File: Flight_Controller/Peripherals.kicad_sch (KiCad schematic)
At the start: 18 parts, among them IC1 AT7456E, U2 BMI270, U4 W25Q128JVSIQ TR, Y2 ABM3-27.000MHZ-D2Y-T

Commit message: Schem V1 Done!
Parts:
- removed R2: 1kΩ, PCM_JLCPCB:R_0603, symbol PCM_JLCPCB-Resistors:0603,1kΩ
- added C10: 33nF, PCM_JLCPCB:C_0603, symbol PCM_JLCPCB-Capacitors:0603,33nF
- added C11, C24, C30, C31, C32, C7: 100nF, PCM_JLCPCB:C_0603, symbol PCM_JLCPCB-Capacitors:0603,100nF
- added C12: 6.8pF, PCM_JLCPCB:C_0603, symbol PCM_JLCPCB-Capacitors:0603,6.8pF
- added C13: 47uF, PCM_JLCPCB:C_0805, symbol PCM_JLCPCB-Capacitors:0805,47uF
- added C14, C15: 1uF, PCM_JLCPCB:C_0603, symbol PCM_JLCPCB-Capacitors:0603,1uF
- added C33: 10uF, PCM_JLCPCB:C_0805, symbol PCM_JLCPCB-Capacitors:0805,10uF,(2)
- added L1: 12uH, symbol Device:L
- added NT1, NT2, NT3, NT4: NetTie_2, symbol Device:NetTie_2
- added R7: 52.3K, symbol Device:R
- added R8: 10kΩ, PCM_JLCPCB:R_0603, symbol PCM_JLCPCB-Resistors:0603,10kΩ
- added U3: TLV75533PDBV, Package_TO_SOT_SMD:SOT-23-5, symbol Regulator_Linear:TLV75533PDBV
- added U5: TPS62932, Package_TO_SOT_SMD:SOT-583-8, symbol Regulator_Switching:TPS62932
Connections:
- net SPI_CLK is gone; now on net SPI_SCK: U4.6 (CLK)
- net SPI_IO0 is gone; now on net SPI_SDI: U4.5 (DI(IO0))
- net +3V3: now also R1.1, R3.1, U2.8 (VDD), C15.1, C24.1, U3.5 (OUT); no longer U2.12 (CSB)
- net +5V: now also C12.1, C13.1, C14.1, C32.1, L1.2, NT1.2, NT2.2, R7.1, U3.1 (IN), U3.3 (EN); no longer R1.1, R3.1
- net +5V_A: now also C31.1, NT1.1
- net +5V_D: now also C30.1, NT2.1
- net GND: now also C10.2, C13.2, C14.2, C15.2, C24.2, C32.2, C33.2, C7.2, NT3.2, NT4.2, R8.2, U3.2 (GND), U5.4 (GND); no longer A1.5 (SDO/SA0), U2.1 (SDO)
- net GNDA: now also C31.2, NT3.1
- net GNDD: now also C30.2, NT4.1
- net CLKIN: now reaches IC1.5 (CLKIN), Y2.1
- net XFB: now reaches IC1.6 (XFB), Y2.2
- net +1V8 renamed LPS_SPI_CS
- net AT_CLKOUT: no longer names the net of IC1.7 (CLKOUT)
- net AT_CS renamed OSD_SPI_CS
- net AT_HS: no longer names the net of IC1.18 (~{HSYNC})
- net AT_LOS renamed OSD_LOS
- net AT_SCLK renamed SPI_SCK
- net SPI_SCK: now also A1.2 (SCL/SPC)
- net AT_SDIN renamed SPI_SDI
- net SPI_SDI: now also A1.4 (SDA/SDI/SDO)
- net AT_SDOUT renamed SPI_SDO
- net SPI_SDO: now also A1.5 (SDO/SA0), U4.2 (DO(IO1))
- net AT_VS renamed OSD_VS
- net BMI_INT renamed IMU_INT
- net SCL renamed IMU_SPI_SCK
- net IMU_SPI_SCK: no longer A1.4 (SDA/SDI/SDO)
- net SDA renamed IMU_SPI_SDI
- net IMU_SPI_SDI: no longer A1.2 (SCL/SPC)
- net SPI_IO1 renamed BB_SPI_CS
- net BB_SPI_CS: no longer U4.2 (DO(IO1))
- new net: C10.1, U5.7 (SS)
- new net +BATT: C33.1, C7.1, U5.3 (VIN)
- new net BMI_SPI_CS: U2.12 (CSB)
- new net BST: C11.1, U5.6 (BST)
- new net FB: C12.2, R7.2, R8.1, U5.8 (FB)
- new net IMU_SPI_SDO: U2.1 (SDO)
- new net SW: C11.2, L1.1, U5.5 (SW)
- no-connect marks 13 -> 17
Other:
- note added: "BAROMETER"
- note added: "BLACKBOX"
- note added: "OSD"
- note added: "POWER"
- moved on the sheet: C1, C2, C3, C6, C8, C9, IC1, R1, R3, R4, R5, Y2

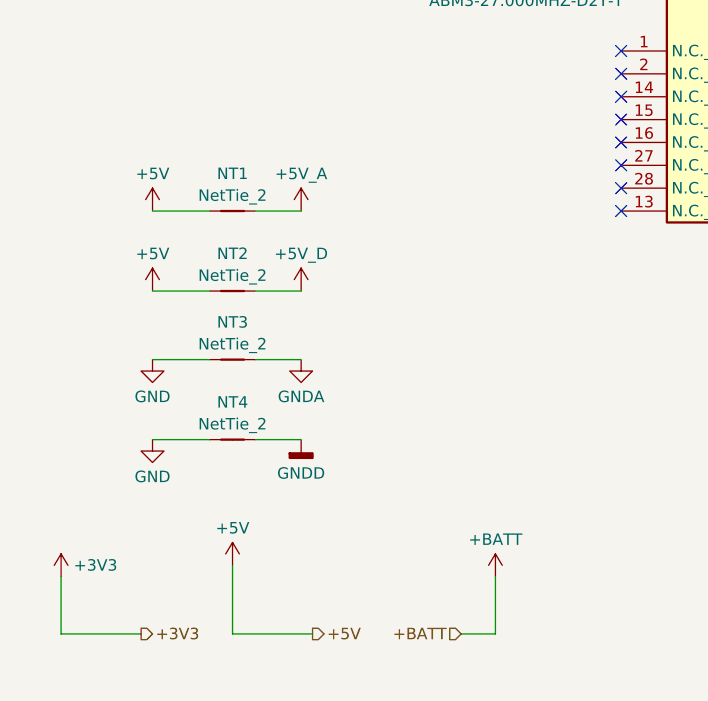
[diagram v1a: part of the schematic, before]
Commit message: Fixed ERC errors
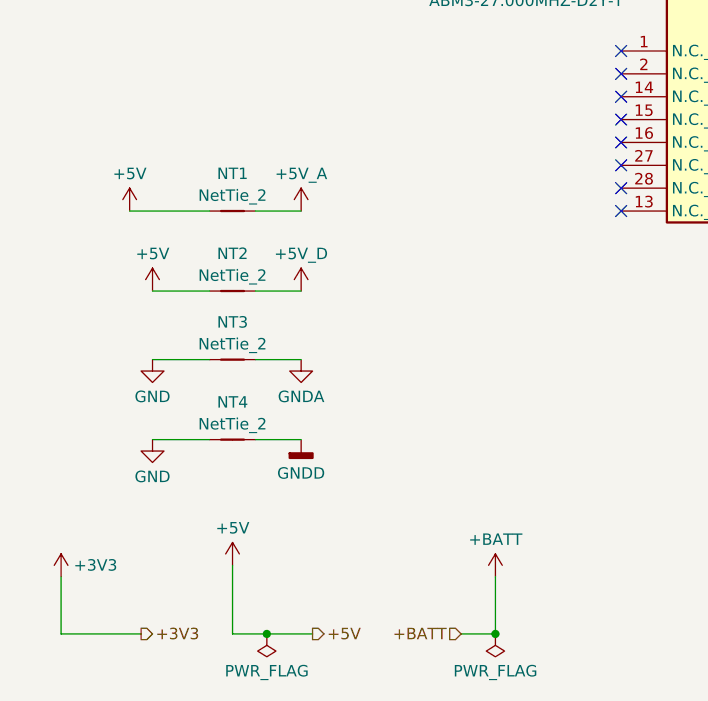
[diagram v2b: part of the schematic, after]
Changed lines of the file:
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@@
 	)
 	(junction
+		(at 66.04 187.96)
+		(diameter 0)
+		(color 0 0 0 0)
+	)
+	(junction
 		(at 127 132.08)
 		(diameter 0)
@@
 	)
 	(junction
+		(at 46.99 99.06)
+		(diameter 0)
+		(color 0 0 0 0)
+	)
+	(junction
 		(at 185.42 57.15)
 		(diameter 0)
@@
 	)
 	(junction
-		(at 46.99 99.06)
-		(diameter 0)
-		(color 0 0 0 0)
-	)
-	(junction
 		(at 31.75 45.72)
 		(diameter 0)
@@
 	)
 	(junction
+		(at 40.64 187.96)
+		(diameter 0)
+		(color 0 0 0 0)
+	)
+	(junction
 		(at 191.77 92.71)
 		(diameter 0)
@@
 	(wire
 		(pts
-			(xy 26.67 187.96) (xy 17.78 187.96)
-		)
-		(stroke
-			(width 0)
-			(type default)
-		)
-	)
-	(wire
-		(pts
 			(xy 54.61 96.52) (xy 54.61 95.25)
 		)
@@
 	(wire
 		(pts
-			(xy 27.94 140.97) (xy 34.29 140.97)
+			(xy 40.64 187.96) (xy 36.83 187.96)
+		)
+		(stroke
+			(width 0)
+			(type default)
+		)
+	)
+	(wire
+		(pts
+			(xy 25.4 140.97) (xy 34.29 140.97)
 		)
 		(stroke
@@
 	(wire
 		(pts
-			(xy 45.72 187.96) (xy 36.83 187.96)
+			(xy 45.72 187.96) (xy 40.64 187.96)
 		)
 		(stroke
@@
 	(wire
 		(pts
+			(xy 17.78 187.96) (xy 26.67 187.96)
+		)
+		(stroke
+			(width 0)
+			(type default)
+		)
+	)
+	(wire
+		(pts
 			(xy 39.37 140.97) (xy 44.45 140.97)
 		)
@@
 		)
 		(instances
-			(project "architecture"
-				(path "/6969013c-8a07-4371-b652-682be13d9ce7/0614acdb-9244-4c03-8409-caeb9c64dc33"
-					(reference "#PWR024")
-					(unit 1)
-				)
-			)
 			(project "Flight_Controller"
 				(path "/75d72a00-cae4-4ac3-9627-df76ad5ec3a2/0614acdb-9244-4c03-8409-caeb9c64dc33"
@@
 		)
 		(instances
-			(project "architecture"
-				(path "/6969013c-8a07-4371-b652-682be13d9ce7/0614acdb-9244-4c03-8409-caeb9c64dc33"
-					(reference "U2")
-					(unit 1)
-				)
-			)
 			(project "Flight_Controller"
 				(path "/75d72a00-cae4-4ac3-9627-df76ad5ec3a2/0614acdb-9244-4c03-8409-caeb9c64dc33"
@@
 		)
 		(instances
-			(project "architecture"
-				(path "/6969013c-8a07-4371-b652-682be13d9ce7/0614acdb-9244-4c03-8409-caeb9c64dc33"
-					(reference "A1")
-					(unit 1)
-				)
-			)
 			(project "Flight_Controller"
 				(path "/75d72a00-cae4-4ac3-9627-df76ad5ec3a2/0614acdb-9244-4c03-8409-caeb9c64dc33"
@@
 	)
 	(symbol
+		(lib_id "power:PWR_FLAG")
+		(at 40.64 187.96 180)
+		(unit 1)
+		(body_style 1)
+		(exclude_from_sim no)
+		(in_bom yes)
+		(on_board yes)
+		(in_pos_files yes)
+		(dnp no)
+		(fields_autoplaced yes)
+		(property "Reference" "#FLG02"
+			(at 40.64 189.865 0)
+			(hide yes)
+			(show_name no)
+			(do_not_autoplace no)
+			(effects
+				(font
+					(size 1.27 1.27)
+				)
+			)
+		)
+		(property "Value" "PWR_FLAG"
+			(at 40.64 192.0931 0)
+			(show_name no)
+			(do_not_autoplace no)
+			(effects
+				(font
+					(size 1.27 1.27)
+				)
+			)
+		)
+		(property "Footprint" ""
+			(at 40.64 187.96 0)
+			(hide yes)
+			(show_name no)
+			(do_not_autoplace no)
+			(effects
+				(font
+					(size 1.27 1.27)
+				)
+			)
+		)
+		(property "Datasheet" ""
+			(at 40.64 187.96 0)
+			(hide yes)
+			(show_name no)
+			(do_not_autoplace no)
+			(effects
+				(font
+					(size 1.27 1.27)
+				)
+			)
+		)
+		(property "Description" "Special symbol for telling ERC where power comes from"
+			(at 40.64 187.96 0)
+			(hide yes)
+			(show_name no)
+			(do_not_autoplace no)
+			(effects
+				(font
+					(size 1.27 1.27)
+				)
+			)
+		)
+		(pin "1"
+		)
+		(instances
+			(project "Flight_Controller"
+				(path "/75d72a00-cae4-4ac3-9627-df76ad5ec3a2/0614acdb-9244-4c03-8409-caeb9c64dc33"
+					(reference "#FLG02")
+					(unit 1)
+				)
+			)
+		)
+	)
+	(symbol
 		(lib_id "PCM_JLCPCB-Capacitors:0805,10uF,(2)")
 		(at 182.88 106.68 0)
@@
 		)
 		(instances
-			(project "architecture"
-				(path "/6969013c-8a07-4371-b652-682be13d9ce7/0614acdb-9244-4c03-8409-caeb9c64dc33"
-					(reference "C9")
-					(unit 1)
-				)
-			)
 			(project "Flight_Controller"
 				(path "/75d72a00-cae4-4ac3-9627-df76ad5ec3a2/0614acdb-9244-4c03-8409-caeb9c64dc33"
@@
 		)
 		(instances
-			(project "architecture"
-				(path "/6969013c-8a07-4371-b652-682be13d9ce7/0614acdb-9244-4c03-8409-caeb9c64dc33"
-					(reference "#PWR014")
-					(unit 1)
-				)
-			)
 			(project "Flight_Controller"
 				(path "/75d72a00-cae4-4ac3-9627-df76ad5ec3a2/0614acdb-9244-4c03-8409-caeb9c64dc33"
@@
 		)
 		(instances
-			(project "architecture"
-				(path "/6969013c-8a07-4371-b652-682be13d9ce7/0614acdb-9244-4c03-8409-caeb9c64dc33"
-					(reference "#PWR023")
-					(unit 1)
-				)
-			)
 			(project "Flight_Controller"
 				(path "/75d72a00-cae4-4ac3-9627-df76ad5ec3a2/0614acdb-9244-4c03-8409-caeb9c64dc33"
@@
 		)
 		(instances
-			(project "architecture"
-				(path "/6969013c-8a07-4371-b652-682be13d9ce7/0614acdb-9244-4c03-8409-caeb9c64dc33"
-					(reference "C6")
-					(unit 1)
-				)
-			)
 			(project "Flight_Controller"
 				(path "/75d72a00-cae4-4ac3-9627-df76ad5ec3a2/0614acdb-9244-4c03-8409-caeb9c64dc33"
@@
 		)
 		(instances
-			(project "architecture"
-				(path "/6969013c-8a07-4371-b652-682be13d9ce7/0614acdb-9244-4c03-8409-caeb9c64dc33"
-					(reference "#PWR011")
-					(unit 1)
-				)
-			)
 			(project "Flight_Controller"
 				(path "/75d72a00-cae4-4ac3-9627-df76ad5ec3a2/0614acdb-9244-4c03-8409-caeb9c64dc33"
@@
 	)
 	(symbol
+		(lib_id "power:PWR_FLAG")
+		(at 66.04 187.96 180)
+		(unit 1)
+		(body_style 1)
+		(exclude_from_sim no)
+		(in_bom yes)
+		(on_board yes)
+		(in_pos_files yes)
+		(dnp no)
+		(fields_autoplaced yes)
+		(property "Reference" "#FLG03"
+			(at 66.04 189.865 0)
+			(hide yes)
+			(show_name no)
+			(do_not_autoplace no)
+			(effects
+				(font
+					(size 1.27 1.27)
+				)
+			)
+		)
+		(property "Value" "PWR_FLAG"
+			(at 66.04 192.0931 0)
+			(show_name no)
+			(do_not_autoplace no)
+			(effects
+				(font
+					(size 1.27 1.27)
+				)
+			)
+		)
+		(property "Footprint" ""
+			(at 66.04 187.96 0)
+			(hide yes)
+			(show_name no)
+			(do_not_autoplace no)
+			(effects
+				(font
+					(size 1.27 1.27)
+				)
+			)
+		)
+		(property "Datasheet" ""
+			(at 66.04 187.96 0)
+			(hide yes)
+			(show_name no)
+			(do_not_autoplace no)
+			(effects
+				(font
+					(size 1.27 1.27)
+				)
+			)
+		)
+		(property "Description" "Special symbol for telling ERC where power comes from"
+			(at 66.04 187.96 0)
+			(hide yes)
+			(show_name no)
+			(do_not_autoplace no)
+			(effects
+				(font
+					(size 1.27 1.27)
+				)
+			)
+		)
+		(pin "1"
+		)
+		(instances
+			(project "Flight_Controller"
+				(path "/75d72a00-cae4-4ac3-9627-df76ad5ec3a2/0614acdb-9244-4c03-8409-caeb9c64dc33"
+					(reference "#FLG03")
+					(unit 1)
+				)
+			)
+		)
+	)
+	(symbol
 		(lib_id "power:GND")
 		(at 214.63 113.03 0)
@@
 	(symbol
 		(lib_id "power:+5V")
-		(at 27.94 140.97 0)
+		(at 25.4 140.97 0)
 		(unit 1)
 		(body_style 1)
@@
 		(fields_autoplaced yes)
 		(property "Reference" "#PWR070"
-			(at 27.94 144.78 0)
+			(at 25.4 144.78 0)
 			(hide yes)
 			(show_name no)
@@
 		)
 		(property "Value" "+5V"
-			(at 27.94 136.8369 0)
+			(at 25.4 136.8369 0)
 			(show_name no)
 			(do_not_autoplace no)
@@
 		)
 		(property "Footprint" ""
-			(at 27.94 140.97 0)
+			(at 25.4 140.97 0)
 			(hide yes)
 			(show_name no)
@@
 		)
 		(property "Datasheet" ""
-			(at 27.94 140.97 0)
+			(at 25.4 140.97 0)
 			(hide yes)
 			(show_name no)
@@
 		)
 		(property "Description" "Power symbol creates a global label with name \"+5V\""
-			(at 27.94 140.97 0)
+			(at 25.4 140.97 0)
 			(hide yes)
 			(show_name no)
@@
 		)
 		(instances
-			(project "architecture"
-				(path "/6969013c-8a07-4371-b652-682be13d9ce7/0614acdb-9244-4c03-8409-caeb9c64dc33"
-					(reference "#PWR022")
-					(unit 1)
-				)
-			)
 			(project "Flight_Controller"
 				(path "/75d72a00-cae4-4ac3-9627-df76ad5ec3a2/0614acdb-9244-4c03-8409-caeb9c64dc33"
@@
 		)
 		(instances
-			(project "architecture"
-				(path "/6969013c-8a07-4371-b652-682be13d9ce7/0614acdb-9244-4c03-8409-caeb9c64dc33"
-					(reference "#PWR020")
-					(unit 1)
-				)
-			)
 			(project "Flight_Controller"
 				(path "/75d72a00-cae4-4ac3-9627-df76ad5ec3a2/0614acdb-9244-4c03-8409-caeb9c64dc33"
@@
 		)
 		(instances
-			(project "architecture"
-				(path "/6969013c-8a07-4371-b652-682be13d9ce7/0614acdb-9244-4c03-8409-caeb9c64dc33"
-					(reference "C8")
-					(unit 1)
-				)
-			)
 			(project "Flight_Controller"
 				(path "/75d72a00-cae4-4ac3-9627-df76ad5ec3a2/0614acdb-9244-4c03-8409-caeb9c64dc33"
@@
 		)
 		(instances
-			(project "architecture"
-				(path "/6969013c-8a07-4371-b652-682be13d9ce7/0614acdb-9244-4c03-8409-caeb9c64dc33"
-					(reference "#PWR01")
-					(unit 1)
-				)
-			)
 			(project "Flight_Controller"
 				(path "/75d72a00-cae4-4ac3-9627-df76ad5ec3a2/0614acdb-9244-4c03-8409-caeb9c64dc33"

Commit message: Set footprints
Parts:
- L1: footprint (none) -> Inductor_SMD:L_TDK_VLS6045EX_VLS6045AF
- NT1, NT2, NT3, NT4: footprint (none) -> NetTie:NetTie-2_THT_Pad1.0mm
- R7: footprint (none) -> PCM_JLCPCB:R_0603

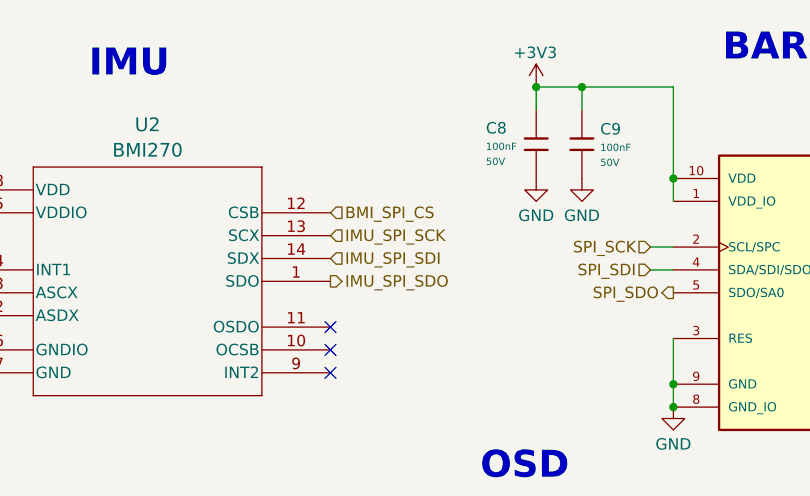
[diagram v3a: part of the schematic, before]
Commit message: Made schem look nicer
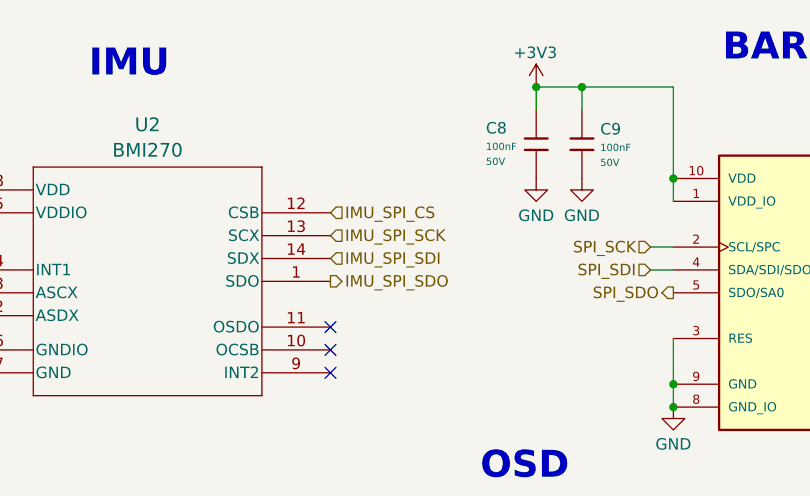
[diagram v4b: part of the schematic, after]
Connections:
- net BMI_SPI_CS renamed IMU_SPI_CS
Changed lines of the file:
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@@
 		)
 	)
-	(hierarchical_label "BMI_SPI_CS"
+	(hierarchical_label "IMU_SPI_CS"
 		(shape input)
 		(at 76.2 49.53 0)

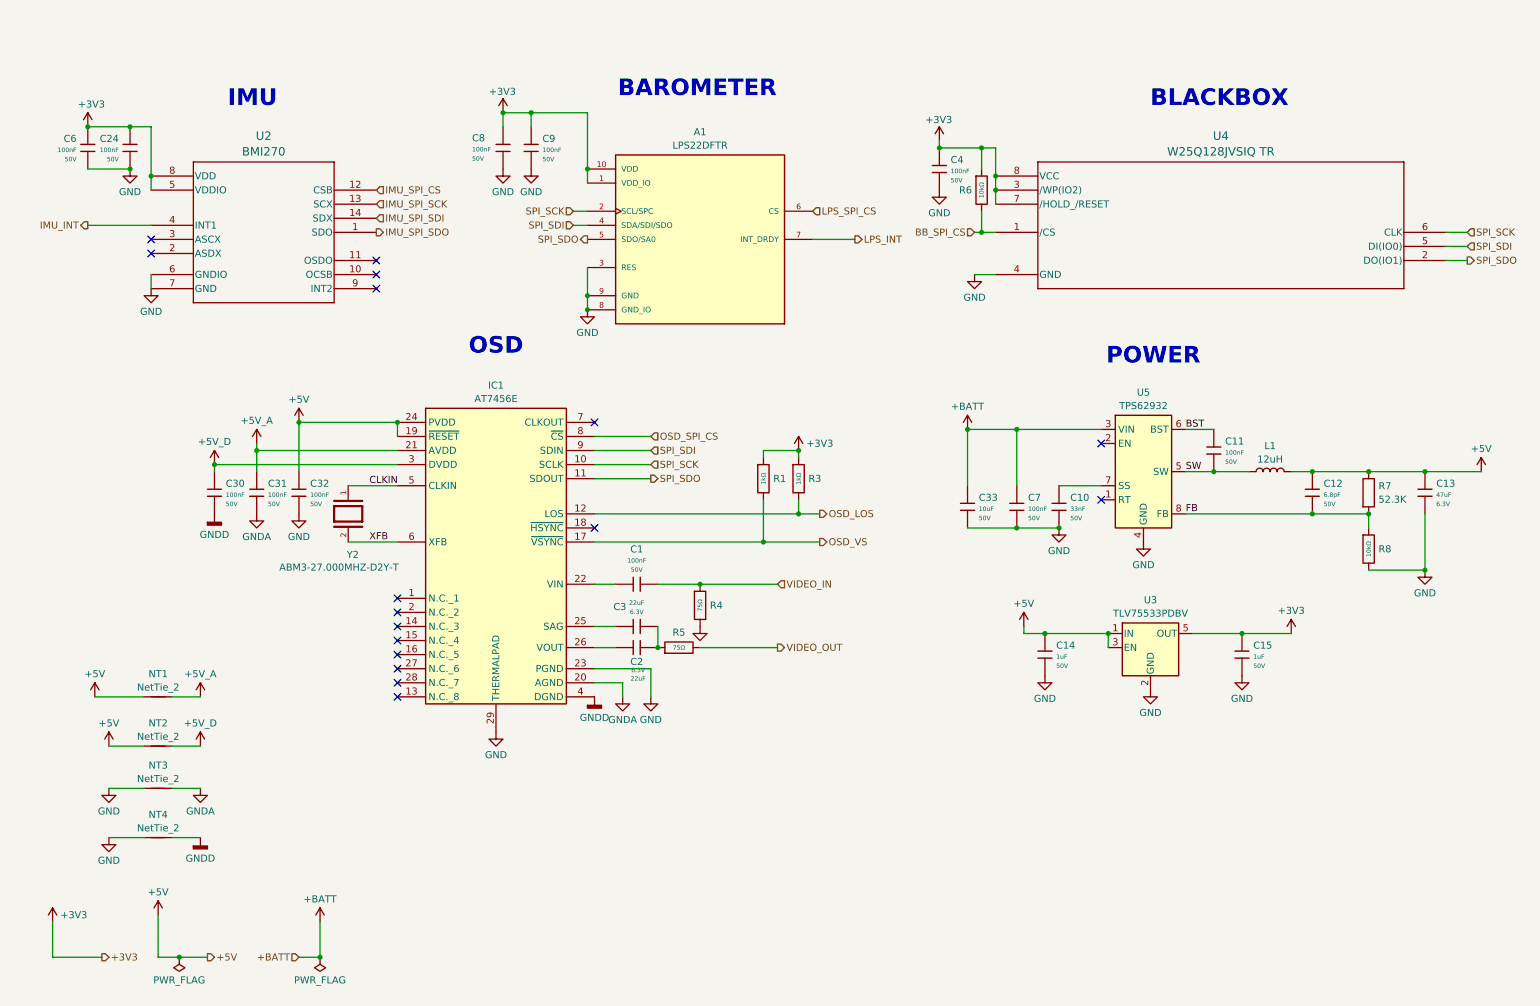
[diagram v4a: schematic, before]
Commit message: Added labels in schem
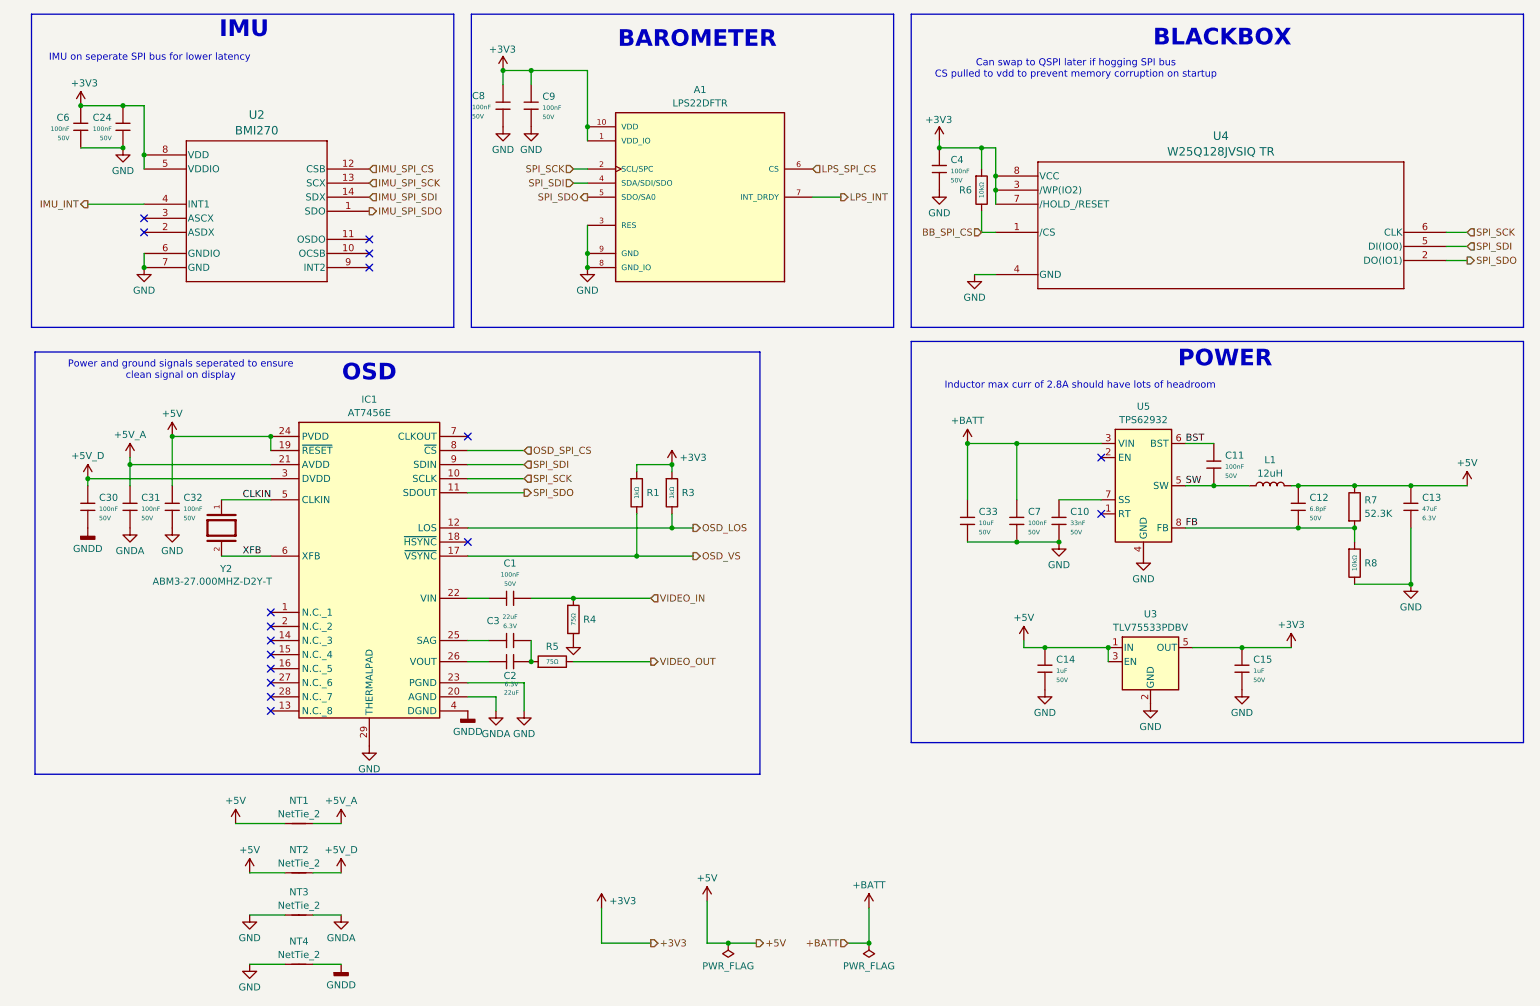
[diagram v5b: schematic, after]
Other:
- note added: "Can swap to QSPI later if hogging SPI bus CS pulled to vdd to prevent memory corruption on startup"
- note added: "IMU on seperate SPI bus for lower latency"
- note added: "Inductor max curr of 2.8A should have lots of headroom"
- note added: "Power and ground signals seperated to ensure clean signal on display"
- moved on the sheet: A1, C1, C10, C11, C12, C13, C14, C15, C2, C24, C3, C30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
